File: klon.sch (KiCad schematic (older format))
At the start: 69 parts, among them SW1 SW_DPDT_x2, U1 TL072, U2 LTC1044, U3 TL072

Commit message: update footprints, values
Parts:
- removed C11, C14, C17: 1u, Capacitor_THT:CP_Radial_D4.0mm_P2.00mm, symbol Device:CP
- removed C12, C22: 4.7u, Capacitor_THT:CP_Radial_D6.3mm_P2.50mm, symbol Device:CP
- added C10, C14, C17: 1u, Capacitor_THT:C_Rect_L7.0mm_W4.5mm_P5.00mm, symbol Device:C
- added C12, C22: 4.7u, Capacitor_THT:C_Rect_L7.0mm_W6.5mm_P5.00mm, symbol Device:C
- C1, C4: footprint Capacitor_THT:C_Rect_L7.0mm_W4.5mm_P5.00mm -> Capacitor_THT:C_Rect_L7.0mm_W2.0mm_P5.00mm
- C11: renamed from C10; value 82n -> 0.082u; footprint Capacitor_THT:C_Rect_L7.0mm_W4.5mm_P5.00mm -> (none)
- C13, C20: footprint Capacitor_THT:C_Rect_L7.0mm_W4.5mm_P5.00mm -> (none)
- C15, C16: footprint Capacitor_THT:CP_Radial_D6.3mm_P2.50mm -> (none); symbol Device:CP -> klon-rescue:CP-Device
- C18: value 2.2n -> 2200p; footprint Capacitor_THT:C_Rect_L7.0mm_W4.5mm_P5.00mm -> (none)
- C19: value 27n -> 0.027u; footprint Capacitor_THT:C_Rect_L7.0mm_W4.5mm_P5.00mm -> Capacitor_THT:C_Rect_L7.0mm_W2.0mm_P5.00mm
- C2, C3, C7, C9: footprint Capacitor_THT:CP_Radial_D4.0mm_P2.00mm -> (none); symbol Device:CP -> klon-rescue:CP-Device
- C21: value 3.9n -> 3900p
- C5, C8: value 68n -> 0.068u; footprint Capacitor_THT:C_Rect_L7.0mm_W4.5mm_P5.00mm -> Capacitor_THT:C_Rect_L7.0mm_W3.5mm_P5.00mm
- C6: value 390n -> 0.39u; footprint Capacitor_THT:C_Rect_L7.0mm_W4.5mm_P5.00mm -> (none)
- GAIN_1: symbol Device:R_POT_Dual_Separate -> klon-rescue:R_POT_Dual_Separate-Device
- GAIN_1: renamed from GAIN_2; symbol Device:R_POT_Dual_Separate -> klon-rescue:R_POT_Dual_Separate-Device
- TONE1, VOL1: symbol Device:R_POT -> klon-rescue:R_POT-Device
- renumbered D6 to D3, D3 to D4, D4 to D5, D5 to D6, R30 to R14, R14 to R15, R15 to R16, R16 to R17, R17 to R18, R18 to R19, R19 to R20, R20 to R21, R21 to R22, R22 to R23, R23 to R24, R24 to R25, R25 to R26, R26 to R27, R27 to R28, R28 to R29, R29 to R30, R8 to R7, R7 to R8

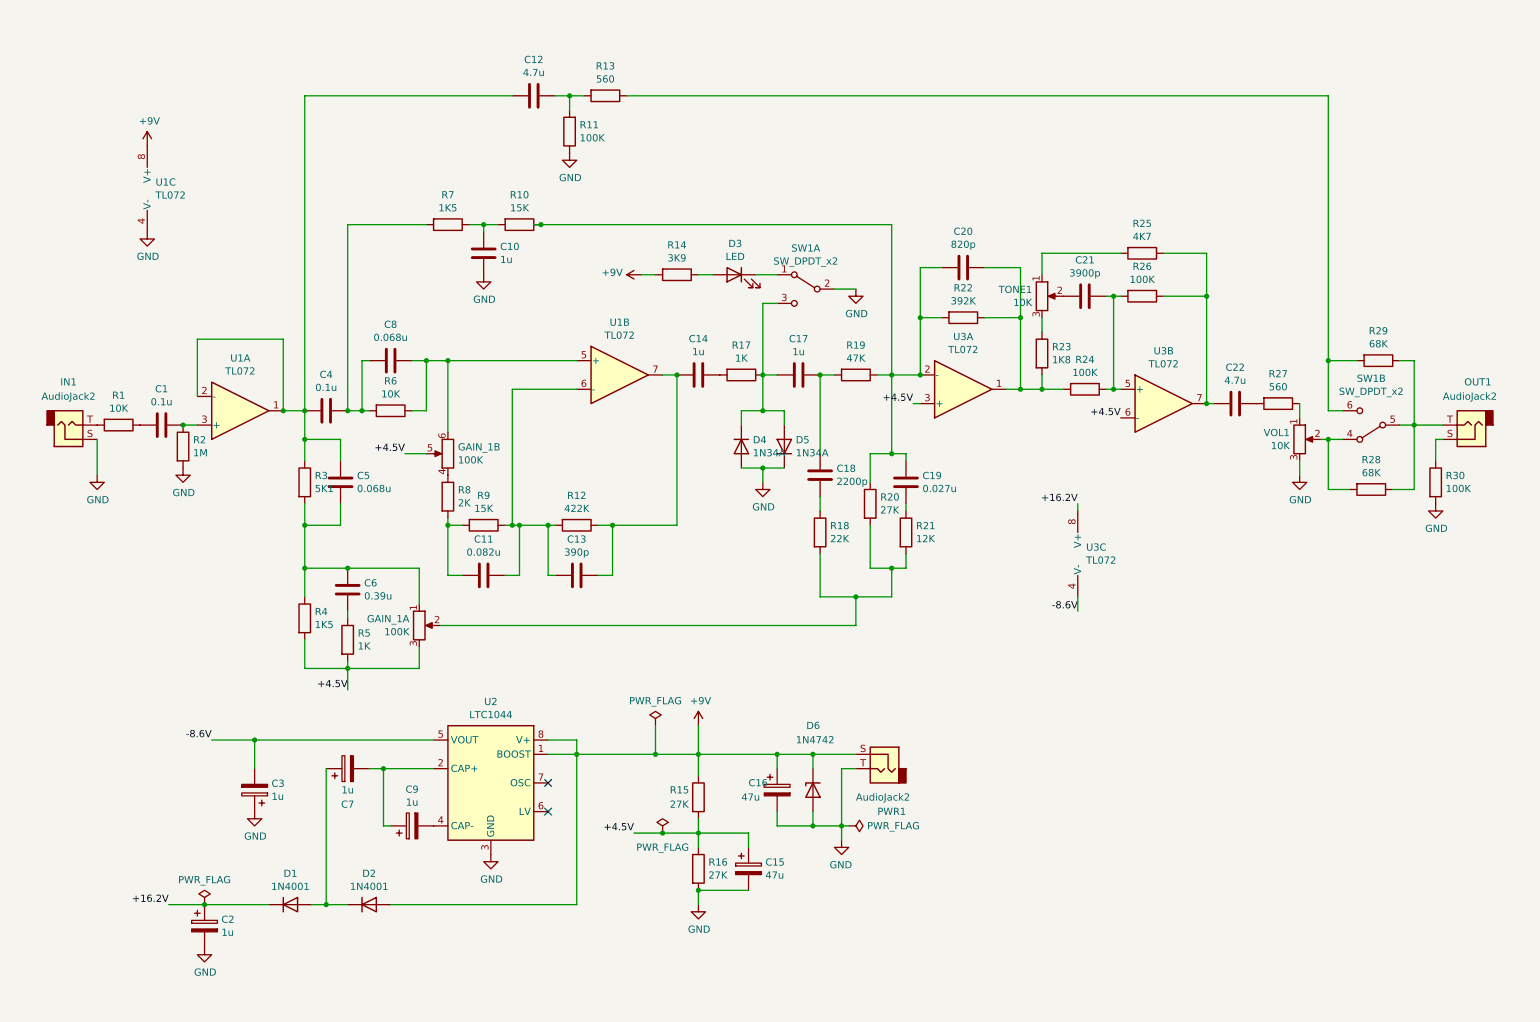
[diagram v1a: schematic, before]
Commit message: update footprints, add bypass LED circuit
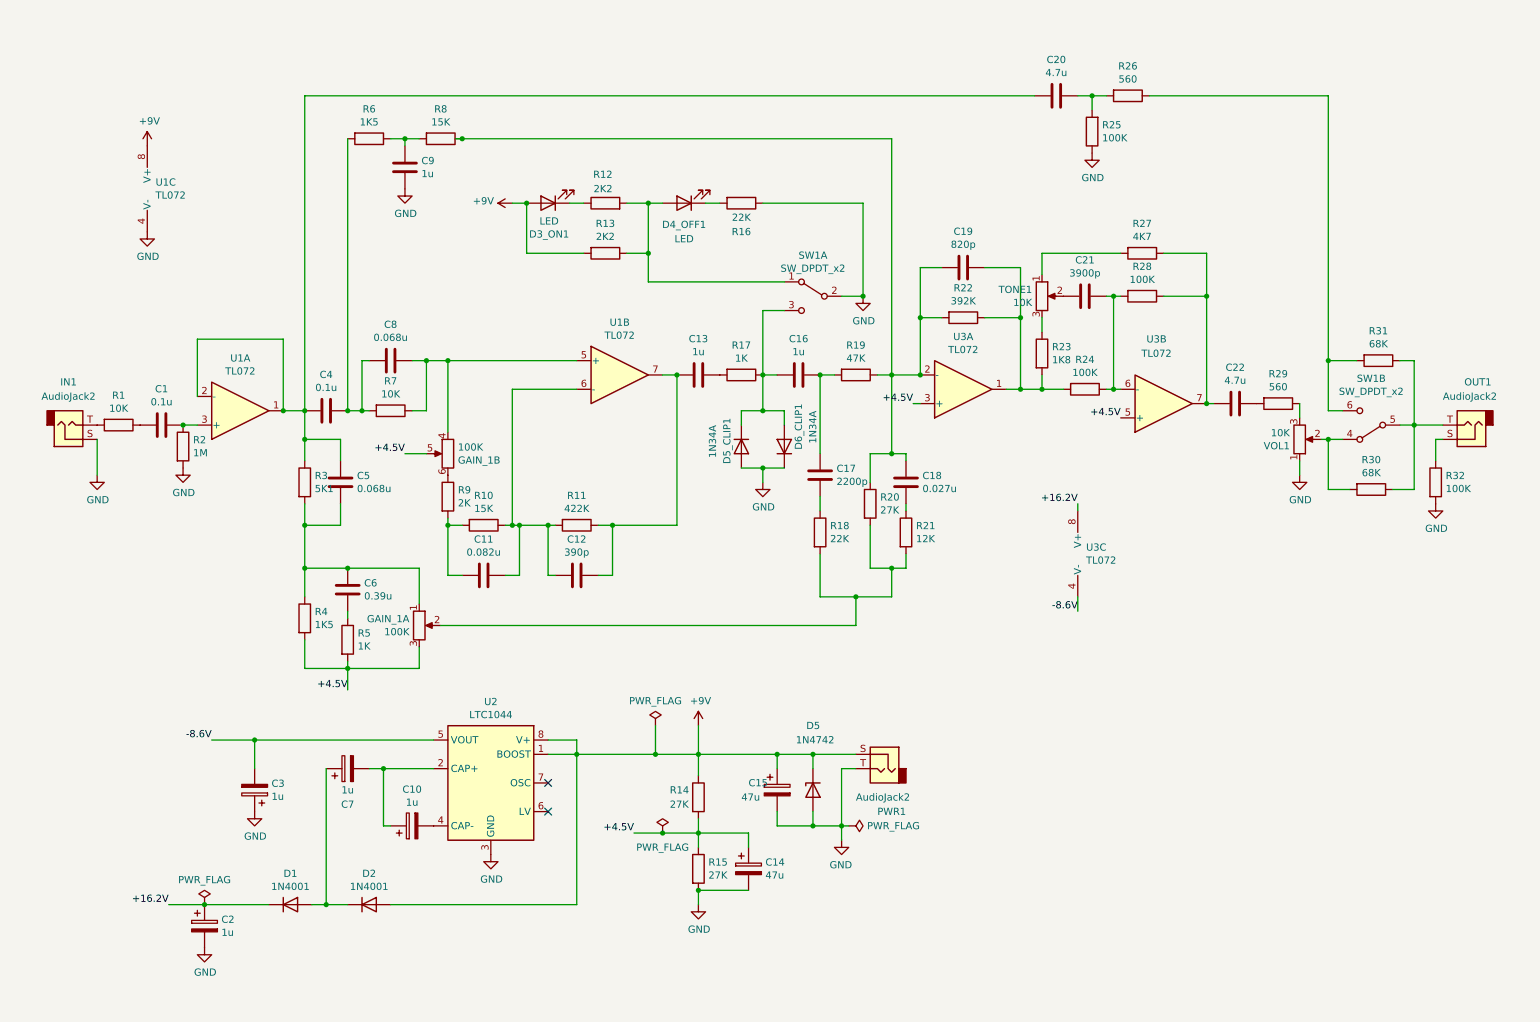
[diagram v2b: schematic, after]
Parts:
- removed R14: 3K9, Resistor_THT:R_Axial_DIN0207_L6.3mm_D2.5mm_P10.16mm_Horizontal, symbol Device:R
- added D4_OFF1: LED, Diode_THT:D_5W_P5.08mm_Vertical_KathodeUp, symbol Device:LED
- added R12, R13: 2K2, Resistor_THT:R_Axial_DIN0207_L6.3mm_D2.5mm_P10.16mm_Horizontal, symbol Device:R
- added R16: 22K, Resistor_THT:R_Axial_DIN0207_L6.3mm_D2.5mm_P10.16mm_Horizontal, symbol Device:R
- C10: renamed from C9; footprint (none) -> Capacitor_THT:CP_Radial_D5.0mm_P2.50mm
- C11: footprint (none) -> Capacitor_THT:C_Rect_L7.0mm_W2.0mm_P5.00mm
- C12: renamed from C13; footprint (none) -> Capacitor_THT:C_Rect_L7.0mm_W4.5mm_P5.00mm
- C14: renamed from C15; footprint (none) -> Capacitor_THT:CP_Radial_D8.0mm_P3.80mm
- C15: renamed from C16; footprint (none) -> Capacitor_THT:CP_Radial_D8.0mm_P3.80mm
- C17: renamed from C18; footprint (none) -> Capacitor_THT:C_Rect_L7.0mm_W2.0mm_P5.00mm
- C19: renamed from C20; footprint (none) -> Capacitor_THT:C_Rect_L7.0mm_W4.5mm_P5.00mm
- C2, C3, C7: footprint (none) -> Capacitor_THT:CP_Radial_D5.0mm_P2.50mm
- C5: footprint Capacitor_THT:C_Rect_L7.0mm_W3.5mm_P5.00mm -> Capacitor_THT:C_Rect_L7.0mm_W2.0mm_P5.00mm
- C6: footprint (none) -> Capacitor_THT:C_Rect_L7.0mm_W4.5mm_P5.00mm
- D5_CLIP1: renamed from D4; footprint Diode_THT:D_5W_P10.16mm_Horizontal -> Diode_THT:D_DO-15_P15.24mm_Horizontal
- D6_CLIP1: renamed from D5; footprint Diode_THT:D_5W_P10.16mm_Horizontal -> Diode_THT:D_DO-15_P15.24mm_Horizontal
- IN1, OUT1: footprint klon:PinHeader_1x02_P1.27mm_Vertical_jack -> Connector_Audio:Jack_6.35mm_Neutrik_NMJ4HFD2_Horizontal
- PWR1: footprint klon:PinHeader_1x02_P1.27mm_Vertical_jack -> Connector_BarrelJack:BarrelJack_Wuerth_6941xx301002
- renumbered C14 to C13, C17 to C16, C19 to C18, C12 to C20, C10 to C9, D3 to D3_ON1, D6 to D5, R9 to R10, R12 to R11, R15 to R14, R16 to R15, R11 to R25, R13 to R26, R25 to R27, R26 to R28, R27 to R29, R28 to R30, R29 to R31, R30 to R32, R7 to R6, R6 to R7, R10 to R8, R8 to R9
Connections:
- net +4.5V: now also U3.5 (+); no longer U3.6 (-)
- net +9V: now also D3_ON1.2 (A), R13.2
- net GND: now also VOL1.1, R16.1; no longer VOL1.3
- net at C8.1, R7.1, U1.5 (+): now also GAIN_1.4; no longer GAIN_1.6
- net at R9.1: now also GAIN_1.6; no longer GAIN_1.4
- net at C21.1, R24.1, R28.2: now also U3.6 (-); no longer U3.5 (+)
- net at R29.1: now also VOL1.3; no longer VOL1.1
- net at D3_ON1.1 (K): now also R12.1; no longer SW1.1 (A)
- new net: D4_OFF1.2 (A), R12.2, R13.1, SW1.1 (A)
- new net: D4_OFF1.1 (K), R16.2
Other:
- moved on the sheet: C20, C9, D3_ON1, R25, R26, R6, R8, SW1A

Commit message: add PCB layout
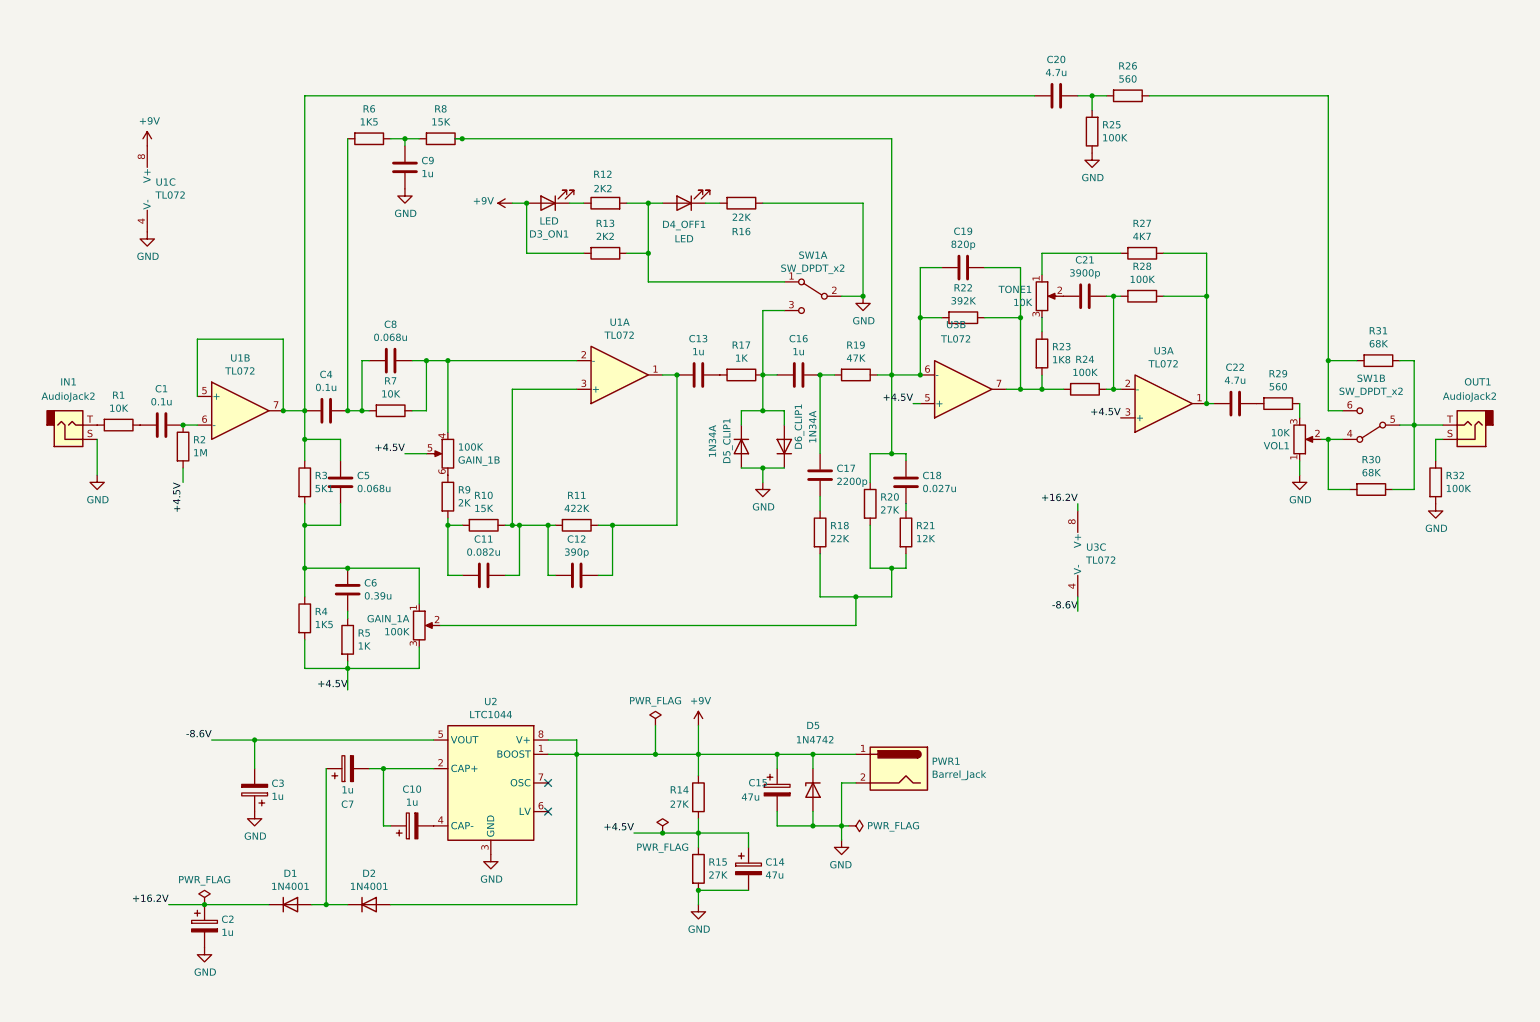
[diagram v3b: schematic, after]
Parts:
- removed PWR1: AudioJack2, Connector_BarrelJack:BarrelJack_Wuerth_6941xx301002, symbol Connector:AudioJack2
- added PWR1: Barrel_Jack, Connector_BarrelJack:BarrelJack_Wuerth_6941xx301002, symbol Connector:Barrel_Jack
- D1, D2: footprint Diode_THT:D_5W_P10.16mm_Horizontal -> Diode_THT:D_DO-34_SOD68_P10.16mm_Horizontal
- D3_ON1, D4_OFF1: footprint Diode_THT:D_5W_P5.08mm_Vertical_KathodeUp -> LED_THT:LED_D3.0mm_Clear
- D5: footprint Diode_THT:D_5W_P10.16mm_Horizontal -> Diode_THT:D_DO-34_SOD68_P7.62mm_Horizontal
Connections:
- net +4.5V: now also R2.2
- net +9V: now also PWR1.1
- net GND: now also PWR1.2; no longer R2.2
- net at C1.1, R2.1: now also U1.6 (-); no longer U1.3 (+)
- net at C20.1, C4.2, C5.1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: now also U1.5 (+), U1.7; no longer U1.1, U1.2 (-)
- net at C8.1, GAIN_1.4, R7.1: now also U1.2 (-); no longer U1.5 (+)
- net at C11.1, C12.2, R10.1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: now also U1.3 (+); no longer U1.6 (-)
- net at C12.1, C13.2, R11.1: now also U1.1; no longer U1.7
- net at C18.1, C19.2, R19.1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: now also U3.6 (-); no longer U3.2 (-)
- net at C19.1, R22.1, R23.2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: now also U3.7; no longer U3.1
- net at C21.1, R24.1, R28.2: now also U3.2 (-); no longer U3.6 (-)
- net at C22.2, R27.1, R28.1: now also U3.1; no longer U3.7
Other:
- moved on the sheet: U1A, U1B, U3A, U3B
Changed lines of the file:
@@
-$EndComp
-$Comp
-L power:GND #PWR04
-U 1 1 60C91B5C
-P 1700 3700
-F 0 "#PWR04" H 1700 3450 50  0001 C CNN
-F 1 "GND" H 1705 3527 50  0000 C CNN
-F 2 "" H 1700 3700 50  0001 C CNN
-F 3 "" H 1700 3700 50  0001 C CNN
-	1    1700 3700
-	1    0    0    -1
 $EndComp
 $Comp
 L Amplifier_Operational:TL072 U1
 U 1 1 60C922E5
+P 4750 3050
+F 0 "U1" H 4750 2683 50  0000 C CNN
+F 1 "TL072" H 4750 2774 50  0000 C CNN
+F 2 "Package_DIP:DIP-8_W7.62mm" H 4750 3050 50  0001 C CNN
+F 3 "http://www.ti.com/lit/ds/symlink/tl071.pdf" H 4750 3050 50  0001 C CNN
+	1    4750 3050
+	1    0    0    1
+$EndComp
+$Comp
+L Amplifier_Operational:TL072 U1
+U 2 1 60C94D46
 P 2100 3300
-F 0 "U1" H 2100 2933 50  0000 C CNN
-F 1 "TL072" H 2100 3024 50  0000 C CNN
+F 0 "U1" H 2100 3667 50  0000 C CNN
+F 1 "TL072" H 2100 3576 50  0000 C CNN
 F 2 "Package_DIP:DIP-8_W7.62mm" H 2100 3300 50  0001 C CNN
 F 3 "http://www.ti.com/lit/ds/symlink/tl071.pdf" H 2100 3300 50  0001 C CNN
-	1    2100 3300
-	1    0    0    1
-$EndComp
-$Comp
-L Amplifier_Operational:TL072 U1
-U 2 1 60C94D46
-P 4750 3050
-F 0 "U1" H 4750 3417 50  0000 C CNN
-F 1 "TL072" H 4750 3326 50  0000 C CNN
-F 2 "Package_DIP:DIP-8_W7.62mm" H 4750 3050 50  0001 C CNN
-F 3 "http://www.ti.com/lit/ds/symlink/tl071.pdf" H 4750 3050 50  0001 C CNN
-	2    4750 3050
+	2    2100 3300
 	1    0    0    -1
 $EndComp
@@
 L Amplifier_Operational:TL072 U3
 U 1 1 60D072A8
-P 7150 3150
-F 0 "U3" H 7150 2783 50  0000 C CNN
-F 1 "TL072" H 7150 2874 50  0000 C CNN
-F 2 "Package_DIP:DIP-8_W7.62mm" H 7150 3150 50  0001 C CNN
-F 3 "http://www.ti.com/lit/ds/symlink/tl071.pdf" H 7150 3150 50  0001 C CNN
-	1    7150 3150
+P 8550 3250
+F 0 "U3" H 8550 2883 50  0000 C CNN
+F 1 "TL072" H 8550 2974 50  0000 C CNN
+F 2 "Package_DIP:DIP-8_W7.62mm" H 8550 3250 50  0001 C CNN
+F 3 "http://www.ti.com/lit/ds/symlink/tl071.pdf" H 8550 3250 50  0001 C CNN
+	1    8550 3250
 	1    0    0    1
 $EndComp
@@
 F 0 "D5" V 5650 5900 50  0000 L CNN
 F 1 "1N4742" V 5750 5800 50  0000 L CNN
-F 2 "Diode_THT:D_5W_P10.16mm_Horizontal" H 6100 5950 50  0001 C CNN
+F 2 "Diode_THT:D_DO-34_SOD68_P7.62mm_Horizontal" H 6100 5950 50  0001 C CNN
 F 3 "~" H 6100 5950 50  0001 C CNN
 	1    6100 5950
@@
 F 0 "D2" H 3000 6967 50  0000 C CNN
 F 1 "1N4001" H 3000 6876 50  0000 C CNN
-F 2 "Diode_THT:D_5W_P10.16mm_Horizontal" H 3000 6750 50  0001 C CNN
+F 2 "Diode_THT:D_DO-34_SOD68_P10.16mm_Horizontal" H 3000 6750 50  0001 C CNN
 F 3 "~" H 3000 6750 50  0001 C CNN
 	1    3000 6750
@@
 F 0 "D1" H 2450 6967 50  0000 C CNN
 F 1 "1N4001" H 2450 6876 50  0000 C CNN
-F 2 "Diode_THT:D_5W_P10.16mm_Horizontal" H 2450 6750 50  0001 C CNN
+F 2 "Diode_THT:D_DO-34_SOD68_P10.16mm_Horizontal" H 2450 6750 50  0001 C CNN
 F 3 "~" H 2450 6750 50  0001 C CNN
 	1    2450 6750
@@
 L Amplifier_Operational:TL072 U3
 U 2 1 60D097BC
-P 8550 3250
-F 0 "U3" H 8500 2800 50  0000 C CNN
-F 1 "TL072" H 8500 2900 50  0000 C CNN
-F 2 "Package_DIP:DIP-8_W7.62mm" H 8550 3250 50  0001 C CNN
-F 3 "http://www.ti.com/lit/ds/symlink/tl071.pdf" H 8550 3250 50  0001 C CNN
-	2    8550 3250
+P 7150 3150
+F 0 "U3" H 7100 2700 50  0000 C CNN
+F 1 "TL072" H 7100 2800 50  0000 C CNN
+F 2 "Package_DIP:DIP-8_W7.62mm" H 7150 3150 50  0001 C CNN
+F 3 "http://www.ti.com/lit/ds/symlink/tl071.pdf" H 7150 3150 50  0001 C CNN
+	2    7150 3150
 	1    0    0    1
 $EndComp
@@
 Wire Wire Line
 	2700 5800 2700 6750
-Connection ~ 3100 5800
-Wire Wire Line
-	3100 5800 3450 5800
 NoConn ~ 4250 5900
 NoConn ~ 4250 6100
@@
 $EndComp
 $Comp
-L Connector:AudioJack2 PWR1
-U 1 1 61A571D6
-P 6600 5800
-F 0 "PWR1" H 6650 5500 50  0000 R CNN
-F 1 "AudioJack2" H 6800 5600 50  0000 R CNN
-F 2 "Connector_BarrelJack:BarrelJack_Wuerth_6941xx301002" H 6600 5800 50  0001 C CNN
-F 3 "~" H 6600 5800 50  0001 C CNN
-	1    6600 5800
-	-1   0    0    -1
-$EndComp
-Wire Wire Line
-	6300 6200 6300 5800
-Wire Wire Line
-	6300 5800 6400 5800
-$Comp
 L Device:C C13
 U 1 1 60DA3D40
@@
 F 0 "D3_ON1" H 4243 2067 50  0000 C CNN
 F 1 "LED" H 4243 1976 50  0000 C CNN
-F 2 "Diode_THT:D_5W_P5.08mm_Vertical_KathodeUp" H 4250 1850 50  0001 C CNN
+F 2 "LED_THT:LED_D3.0mm_Clear" H 4250 1850 50  0001 C CNN
 F 3 "~" H 4250 1850 50  0001 C CNN
 	1    4250 1850
@@
 F 0 "D4_OFF1" H 5200 2000 50  0000 C CNN
 F 1 "LED" H 5200 2100 50  0000 C CNN
-F 2 "Diode_THT:D_5W_P5.08mm_Vertical_KathodeUp" H 5200 1850 50  0001 C CNN
+F 2 "LED_THT:LED_D3.0mm_Clear" H 5200 1850 50  0001 C CNN
 F 3 "~" H 5200 1850 50  0001 C CNN
 	1    5200 1850
 	-1   0    0    1
 $EndComp
+$Comp
+L Connector:Barrel_Jack PWR1
+U 1 1 60E46D62
+P 6700 5800
+F 0 "PWR1" H 6470 5850 50  0000 R CNN
+F 1 "Barrel_Jack" H 6470 5759 50  0000 R CNN
+F 2 "Connector_BarrelJack:BarrelJack_Wuerth_6941xx301002" H 6750 5760 50  0001 C CNN
+F 3 "~" H 6750 5760 50  0001 C CNN
+	1    6700 5800
+	-1   0    0    -1
+$EndComp
+Wire Wire Line
+	6300 6200 6300 5900
+Wire Wire Line
+	6300 5900 6400 5900
+Text Label 1700 3800 3    50   ~ 0
++4.5V
+Wire Wire Line
+	1700 3800 1700 3700
+Connection ~ 3100 5800
+Wire Wire Line
+	3100 5800 3450 5800
 $EndSCHEMATC
